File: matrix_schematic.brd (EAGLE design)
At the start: 84.8 x 82.5 mm, 24 parts, among them IC1 74LS595D, IC2 74LS595D, IC3 74LS595D, Q1 MOSFET-NCHANNELBS270, Q2 MOSFET-NCHANNELBS270, Q3 MOSFET-NCHANNELBS270, Q4 MOSFET-NCHANNELBS270

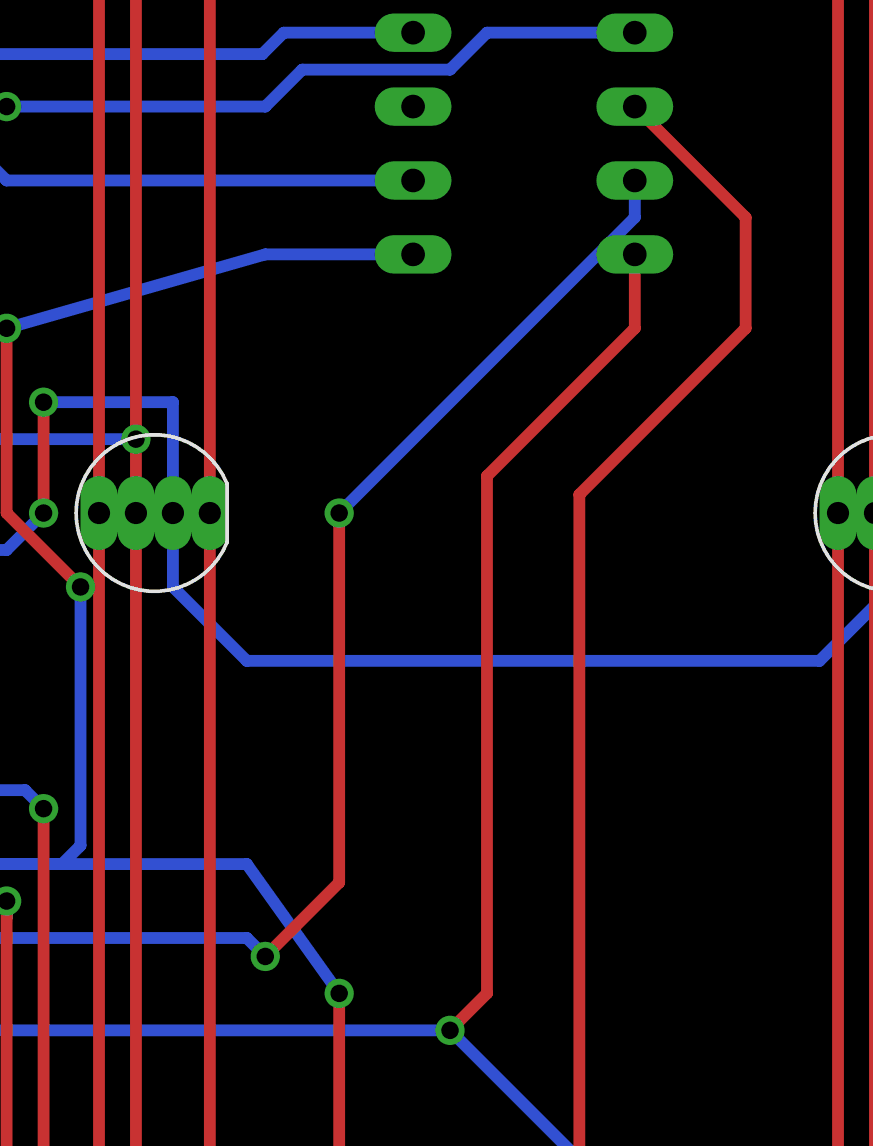
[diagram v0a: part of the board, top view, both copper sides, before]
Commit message: Fixed airwire
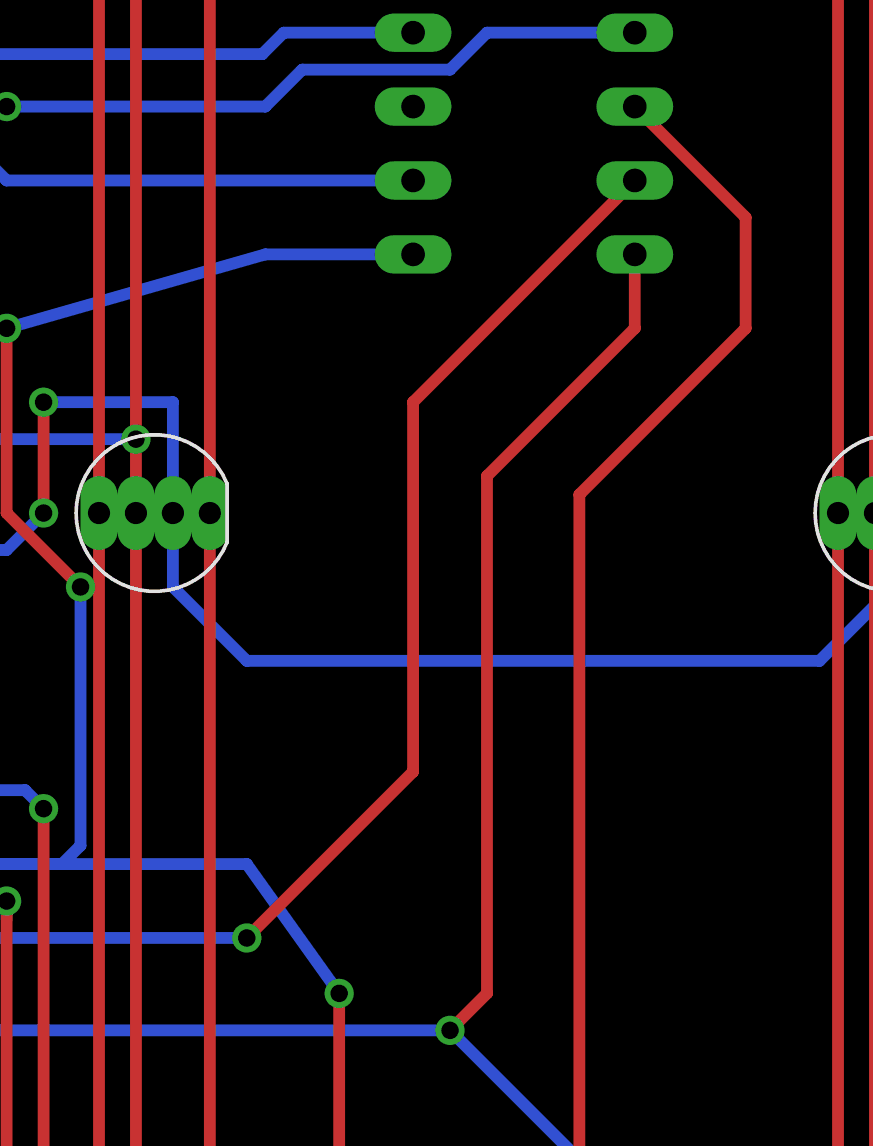
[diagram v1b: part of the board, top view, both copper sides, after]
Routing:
- net N$21: track 45.6 -> 44.4 mm
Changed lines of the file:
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@@
 <setting verticaltext="up"/>
 </settings>
-<grid distance="0.05" unitdist="inch" unit="inch" style="lines" multiple="1" display="yes" altdistance="0.025" altunitdist="inch" altunit="inch"/>
+<grid distance="0.05" unitdist="inch" unit="inch" style="lines" multiple="1" display="no" altdistance="0.025" altunitdist="inch" altunit="inch"/>
 <layers>
 <layer number="1" name="Top" color="4" fill="1" visible="yes" active="yes"/>
@@
 <layer number="23" name="tOrigins" color="15" fill="1" visible="yes" active="yes"/>
 <layer number="24" name="bOrigins" color="15" fill="1" visible="yes" active="yes"/>
-<layer number="25" name="tNames" color="7" fill="1" visible="yes" active="yes"/>
-<layer number="26" name="bNames" color="7" fill="1" visible="yes" active="yes"/>
-<layer number="27" name="tValues" color="7" fill="1" visible="yes" active="yes"/>
-<layer number="28" name="bValues" color="7" fill="1" visible="yes" active="yes"/>
+<layer number="25" name="tNames" color="7" fill="1" visible="no" active="yes"/>
+<layer number="26" name="bNames" color="7" fill="1" visible="no" active="yes"/>
+<layer number="27" name="tValues" color="7" fill="1" visible="no" active="yes"/>
+<layer number="28" name="bValues" color="7" fill="1" visible="no" active="yes"/>
 <layer number="29" name="tStop" color="7" fill="3" visible="no" active="yes"/>
 <layer number="30" name="bStop" color="7" fill="6" visible="no" active="yes"/>
@@
 <layer number="37" name="tTest" color="7" fill="1" visible="no" active="yes"/>
 <layer number="38" name="bTest" color="7" fill="1" visible="no" active="yes"/>
-<layer number="39" name="tKeepout" color="4" fill="11" visible="yes" active="yes"/>
-<layer number="40" name="bKeepout" color="1" fill="11" visible="yes" active="yes"/>
-<layer number="41" name="tRestrict" color="4" fill="10" visible="yes" active="yes"/>
-<layer number="42" name="bRestrict" color="1" fill="10" visible="yes" active="yes"/>
-<layer number="43" name="vRestrict" color="2" fill="10" visible="yes" active="yes"/>
+<layer number="39" name="tKeepout" color="4" fill="11" visible="no" active="yes"/>
+<layer number="40" name="bKeepout" color="1" fill="11" visible="no" active="yes"/>
+<layer number="41" name="tRestrict" color="4" fill="10" visible="no" active="yes"/>
+<layer number="42" name="bRestrict" color="1" fill="10" visible="no" active="yes"/>
+<layer number="43" name="vRestrict" color="2" fill="10" visible="no" active="yes"/>
 <layer number="44" name="Drills" color="7" fill="1" visible="no" active="yes"/>
-<layer number="45" name="Holes" color="7" fill="1" visible="no" active="yes"/>
-<layer number="46" name="Milling" color="3" fill="1" visible="no" active="yes"/>
+<layer number="45" name="Holes" color="7" fill="1" visible="yes" active="yes"/>
+<layer number="46" name="Milling" color="3" fill="1" visible="yes" active="yes"/>
 <layer number="47" name="Measures" color="7" fill="1" visible="no" active="yes"/>
-<layer number="48" name="Document" color="7" fill="1" visible="yes" active="yes"/>
-<layer number="49" name="Reference" color="7" fill="1" visible="yes" active="yes"/>
+<layer number="48" name="Document" color="7" fill="1" visible="no" active="yes"/>
+<layer number="49" name="Reference" color="7" fill="1" visible="no" active="yes"/>
 <layer number="50" name="dxf" color="7" fill="1" visible="no" active="no"/>
-<layer number="51" name="tDocu" color="7" fill="1" visible="yes" active="yes"/>
-<layer number="52" name="bDocu" color="7" fill="1" visible="yes" active="yes"/>
+<layer number="51" name="tDocu" color="7" fill="1" visible="no" active="yes"/>
+<layer number="52" name="bDocu" color="7" fill="1" visible="no" active="yes"/>
 <layer number="53" name="tGND_GNDA" color="7" fill="9" visible="no" active="no"/>
 <layer number="54" name="bGND_GNDA" color="1" fill="9" visible="no" active="no"/>
@@
 <contactref element="IC1" pad="14"/>
 <contactref element="ATTINY85" pad="7"/>
-<wire x1="71.12" y1="64.77" x2="71.12" y2="63.5" width="0.4064" layer="16"/>
-<wire x1="71.12" y1="63.5" x2="60.96" y2="53.34" width="0.4064" layer="16"/>
-<via x="60.96" y="53.34" extent="1-16" drill="0.6" shape="square"/>
-<wire x1="60.96" y1="53.34" x2="60.96" y2="40.64" width="0.4064" layer="1"/>
-<wire x1="60.96" y1="40.64" x2="58.42" y2="38.1" width="0.4064" layer="1"/>
 <wire x1="44.9834" y1="38.735" x2="57.785" y2="38.735" width="0.4064" layer="16"/>
-<wire x1="57.785" y1="38.735" x2="58.42" y2="38.1" width="0.4064" layer="16"/>
-<wire x1="58.42" y1="38.1" x2="58.42" y2="38.1" width="0" layer="19" extent="1-16"/>
+<via x="57.785" y="38.735" extent="1-16" drill="0.6" shape="square"/>
+<wire x1="57.785" y1="38.735" x2="63.5" y2="44.45" width="0.4064" layer="1"/>
+<wire x1="63.5" y1="44.45" x2="63.5" y2="57.15" width="0.4064" layer="1"/>
+<wire x1="63.5" y1="57.15" x2="71.12" y2="64.77" width="0.4064" layer="1"/>
 </signal>
 <signal name="N$22">
@@
 </signal>
 <signal name="N$35">
-<via x="58.42" y="38.1" extent="1-16" drill="0.6" shape="square"/>
 </signal>
 </signals>
